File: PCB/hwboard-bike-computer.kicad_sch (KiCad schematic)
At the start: 0 parts

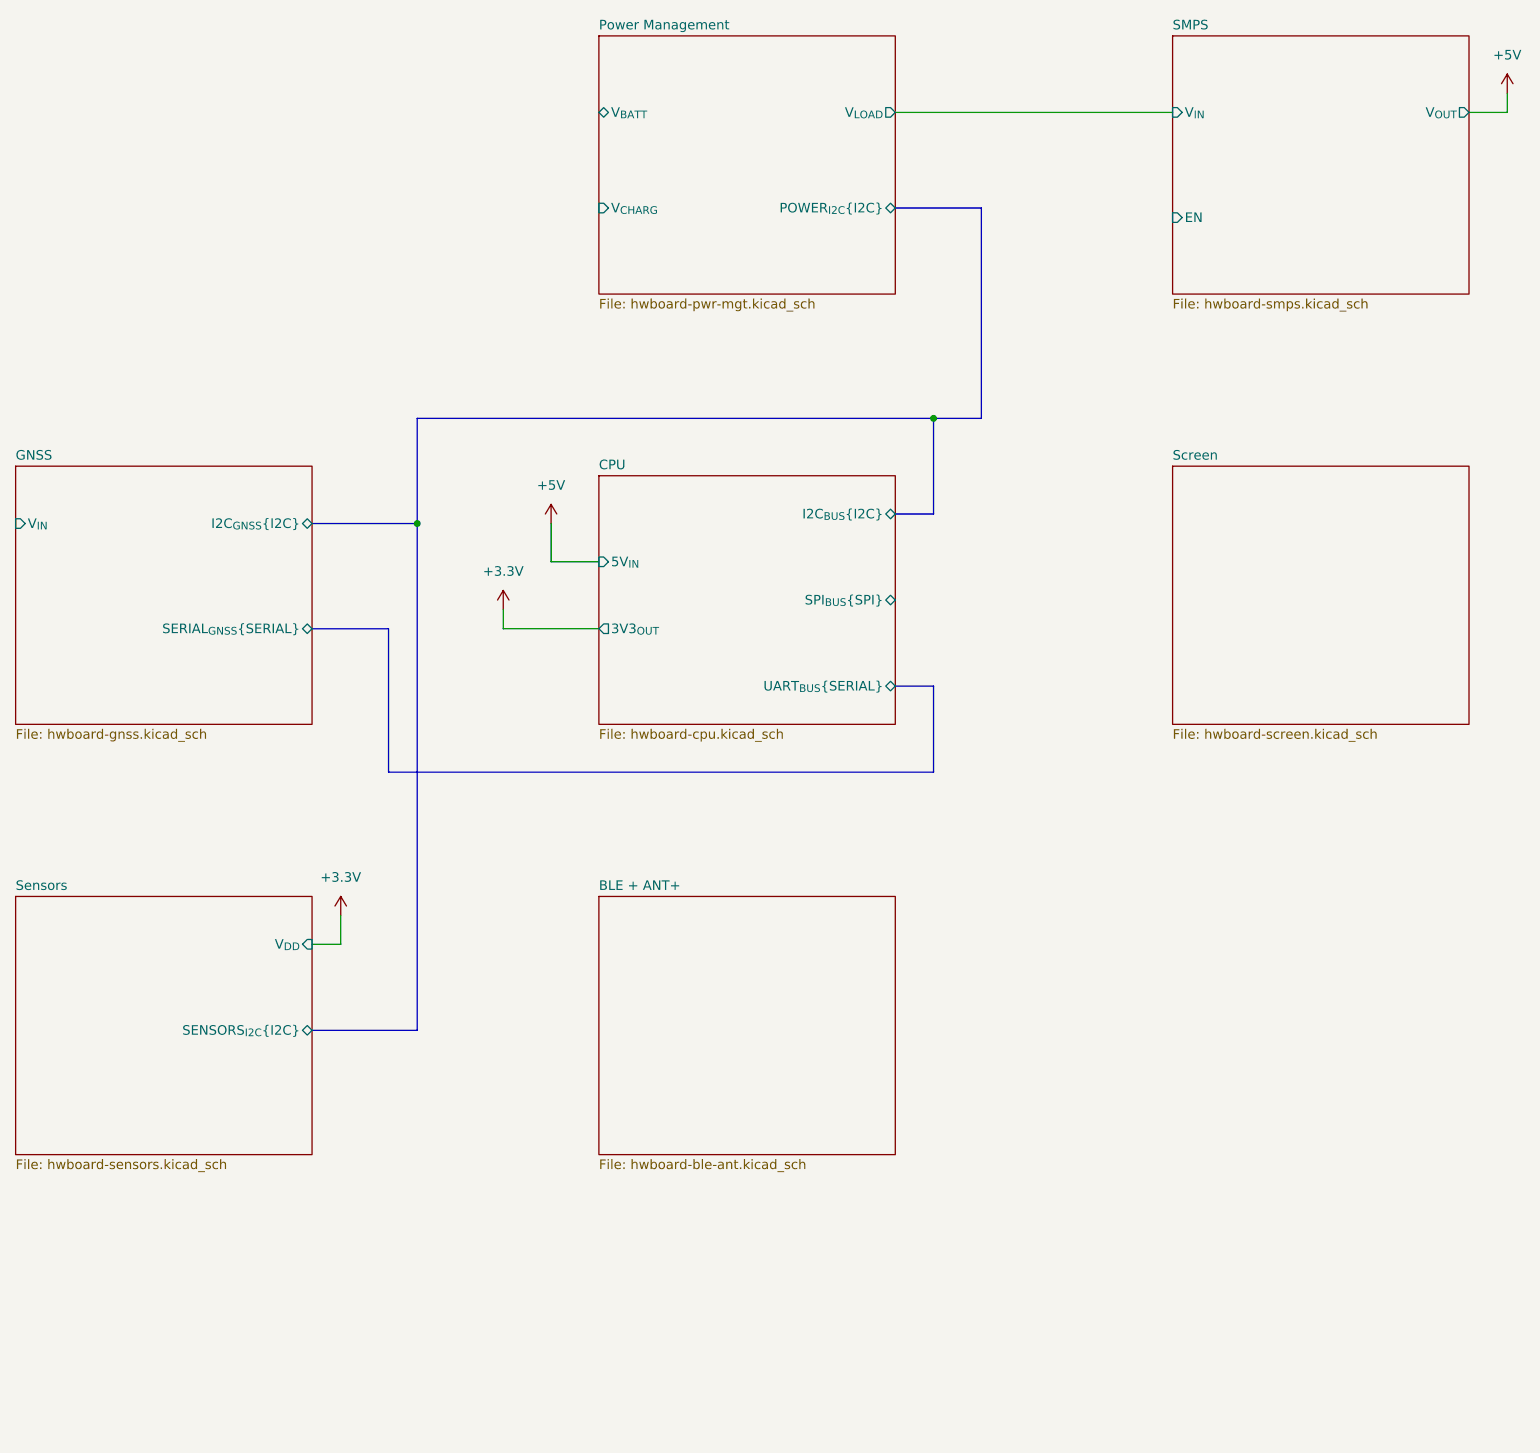
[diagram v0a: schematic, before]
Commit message: add labels
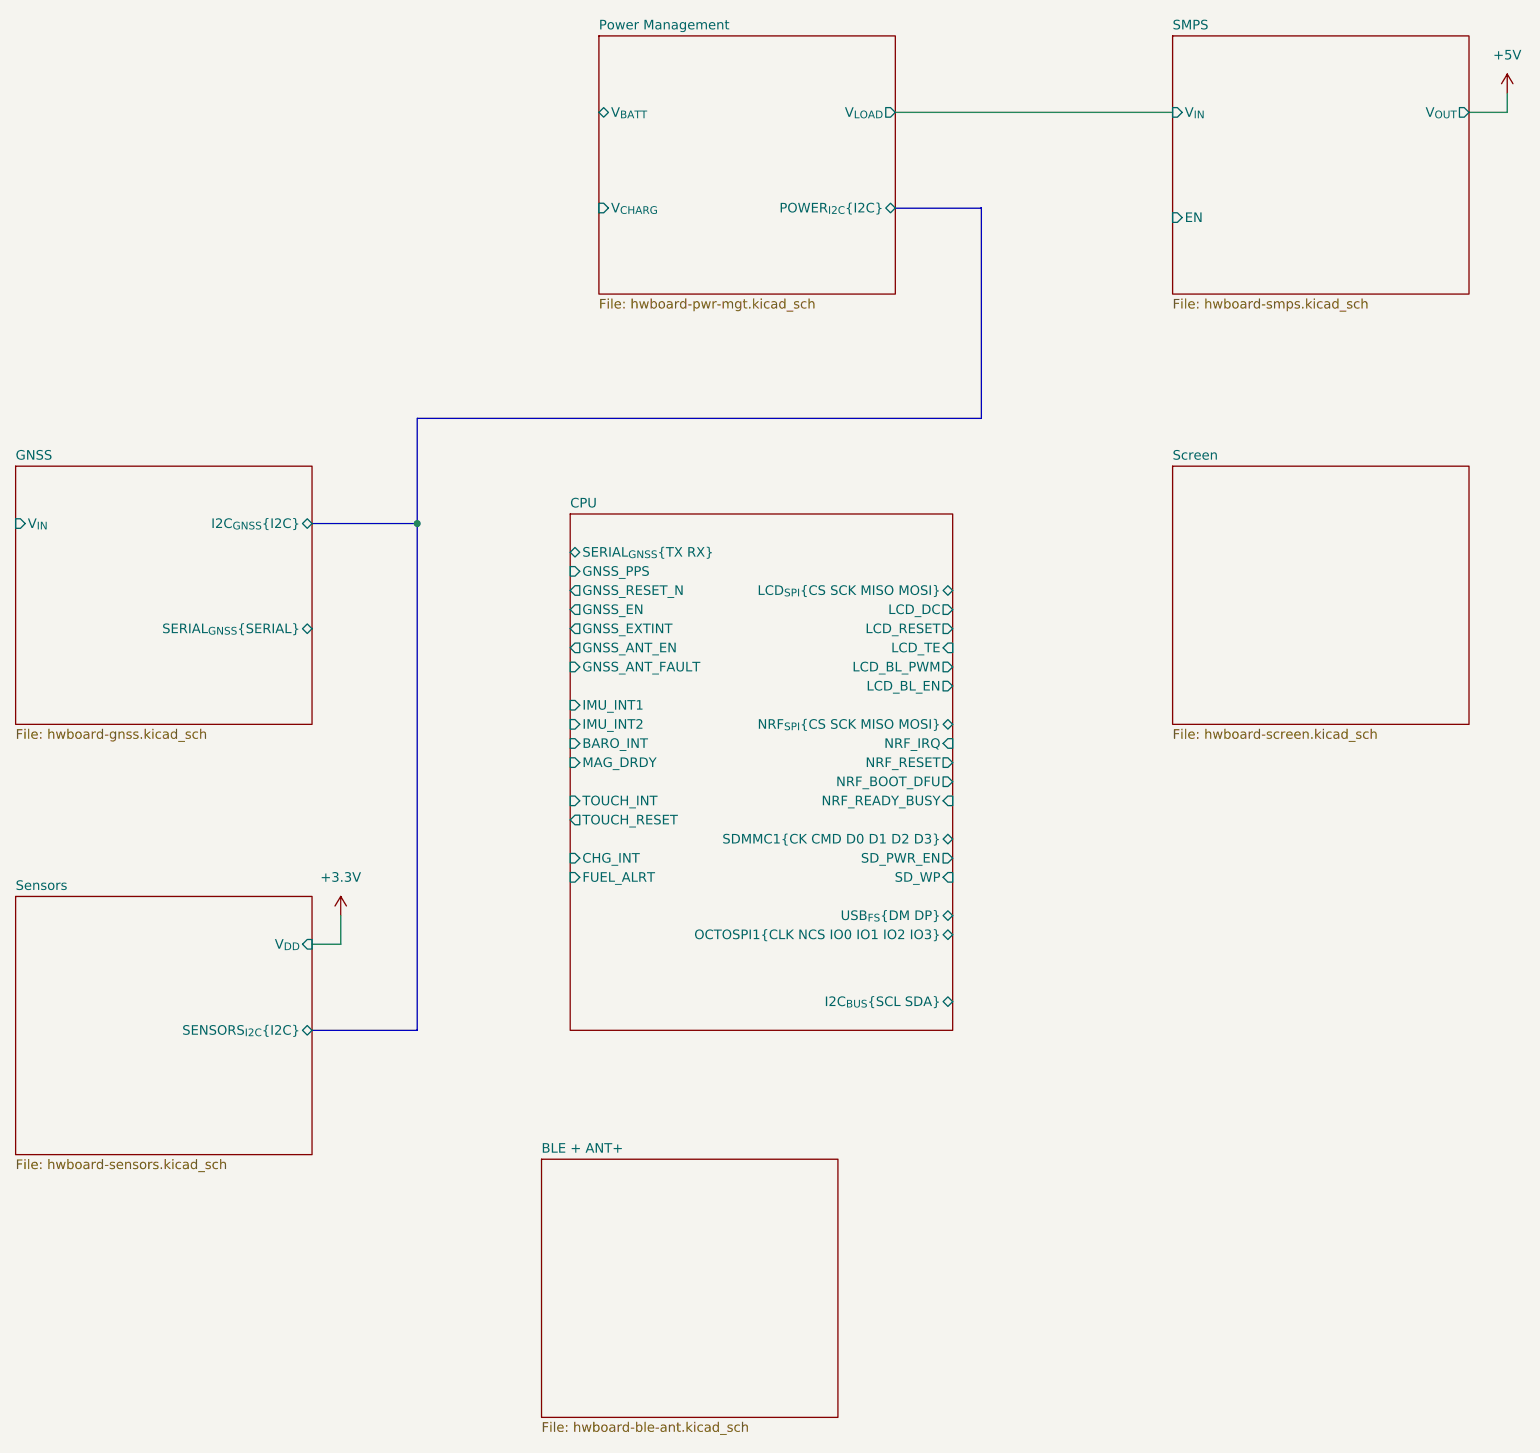
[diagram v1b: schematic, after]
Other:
- sheet CPU ports: added BARO_INT, CHG_INT, FUEL_ALRT, GNSS_ANT_EN, GNSS_ANT_FAULT, GNSS_EN, GNSS_EXTINT, GNSS_PPS, GNSS_RESET_N, I2C_{BUS}{SCL SDA}, IMU_INT1, IMU_INT2, LCD_BL_EN, LCD_BL_PWM, LCD_DC, LCD_RESET, LCD_TE, LCD_{SPI}{CS SCK MISO MOSI}, MAG_DRDY, NRF_BOOT_DFU, NRF_IRQ, NRF_READY_BUSY, NRF_RESET, NRF_{SPI}{CS SCK MISO MOSI}, OCTOSPI1{CLK NCS IO0 IO1 IO2 IO3}, SDMMC1{CK CMD D0 D1 D2 D3}, SD_PWR_EN, SD_WP, SERIAL_{GNSS}{TX RX}, TOUCH_INT, TOUCH_RESET, USB_{FS}{DM DP}; removed 3V3_{OUT}, 5V_{IN}, I2C_{BUS}{I2C}, SPI_{BUS}{SPI}, UART_{BUS}{SERIAL}
